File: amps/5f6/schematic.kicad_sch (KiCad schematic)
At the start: 69 parts, among them T3 2R sec

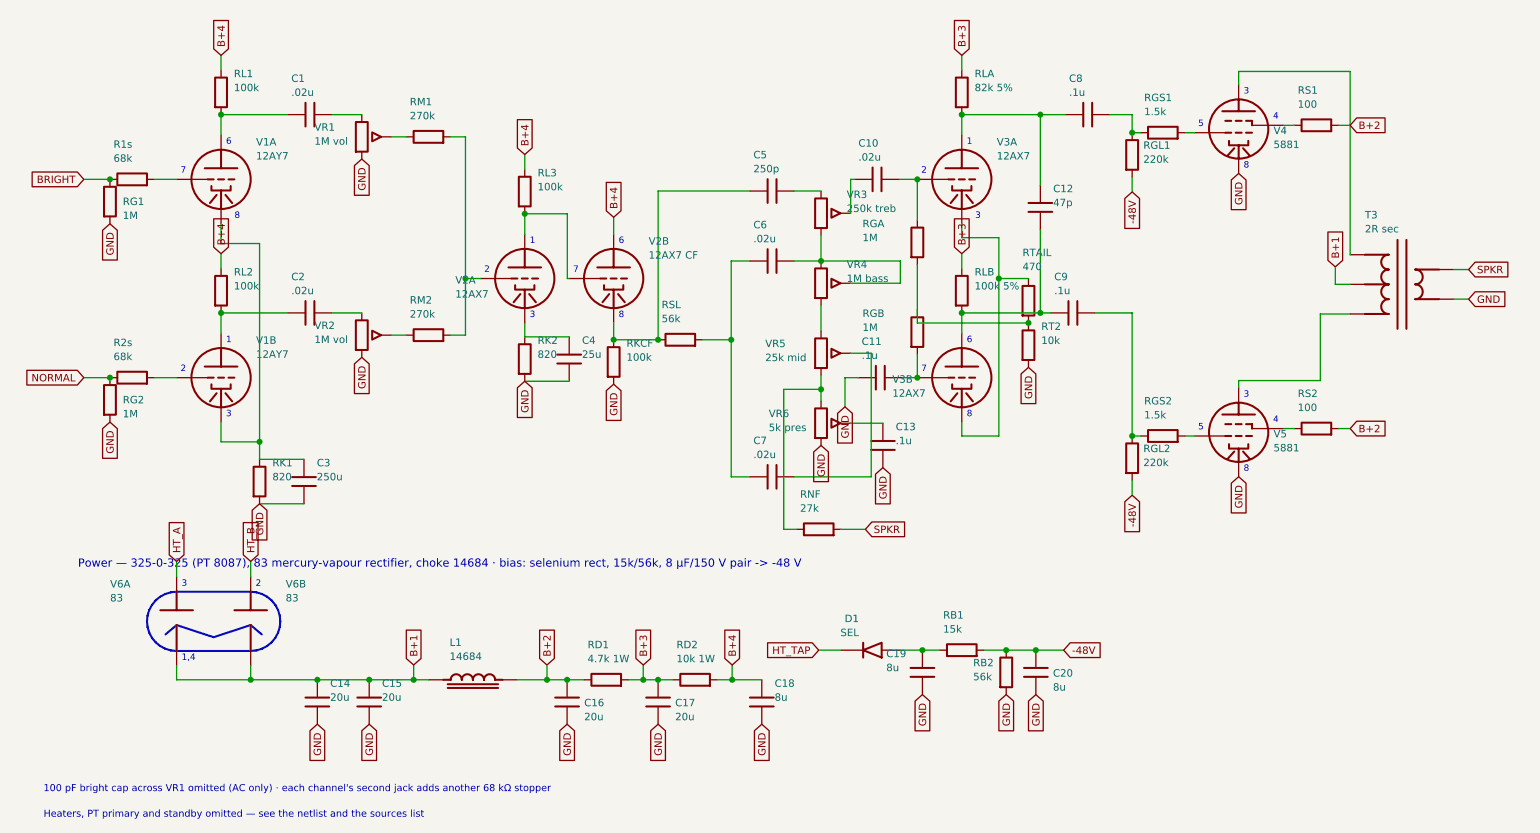
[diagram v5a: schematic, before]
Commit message: 5F6: each input jack has its own 68 kΩ stopper (V1 audit)
F-EG draws four input jacks and four 68 Ks, two per channel, on both pages
(schematic 6039x3508 crop 0,850,1300,2550; layout 6286x3564 crop
4950,450,6000,2250), with each channel's 1 MΩ leak at jack 1's tip. The
corpus carried one 68 K per channel, a simplification the BOM note and the
layout caption stated. R3s and R4s (68 k) are added to the BOM, the sheet
and the board (declared series_bridge); the board widens by two columns.
No DC node moves.

Co-Authored-By: Claude Opus 5.5 <noreply@anthropic.com>
Claude-Session: https://claude.ai/code/session_01KBMfdh37HmCL2iWcBiL5J1
Signed-off-by: AnalogMaker <theanalogmaker@gmail.com>
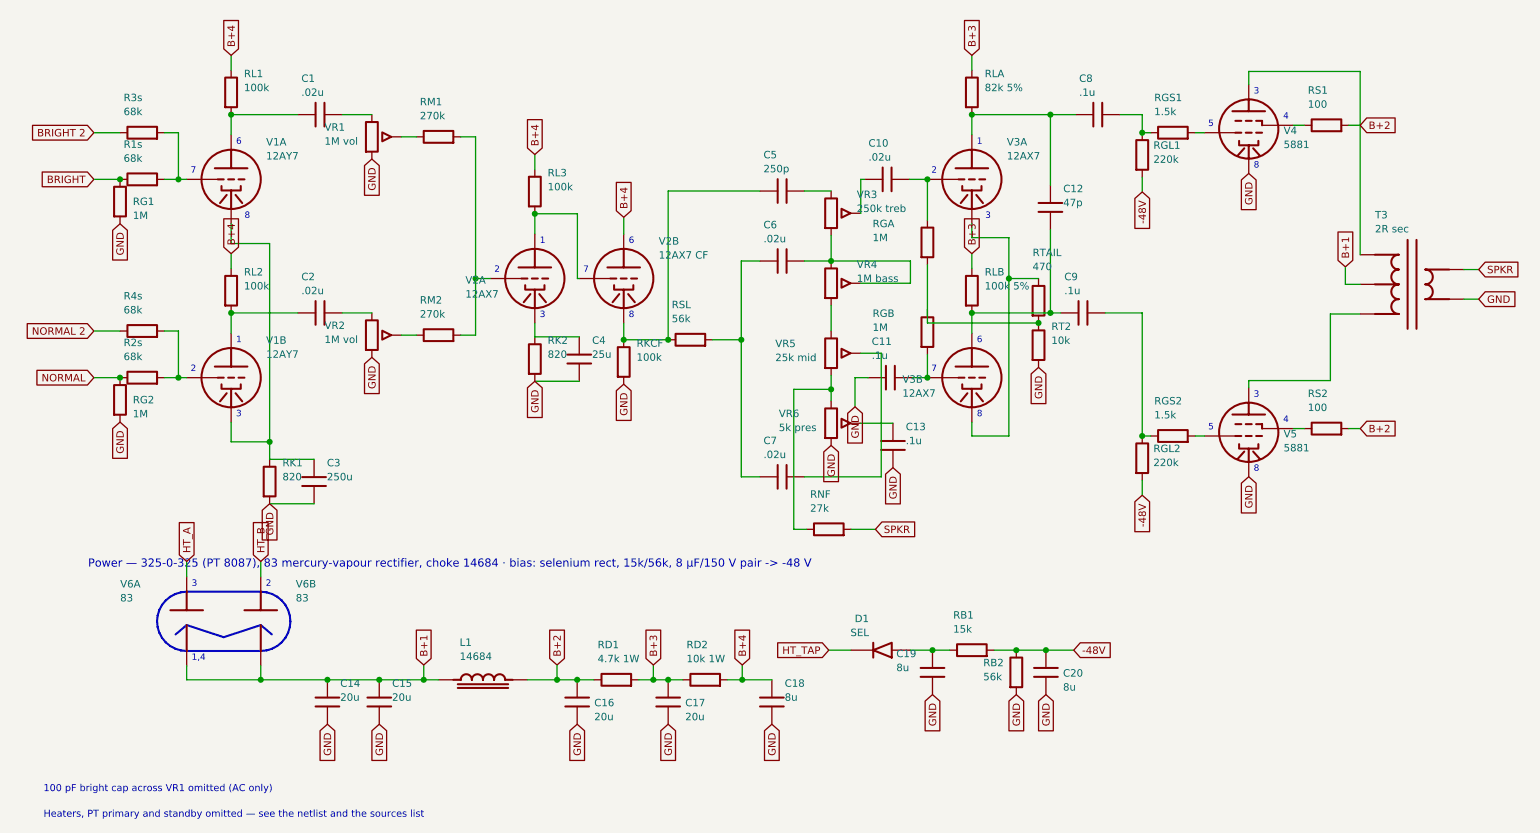
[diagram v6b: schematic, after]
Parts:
- removed C12: 47p, symbol cx:C
- removed C13: .1u, symbol cx:C
- removed D1: SEL, symbol cx:DIODE_SS
- removed RGS1: 1.5k, symbol cx:R
- removed RK1: 820, symbol cx:R
- removed RL1: 100k, symbol cx:R
- removed RLA: 82k 5%, symbol cx:R
- removed V2A: 12AX7, symbol cx:TRIODE
- added C20: 8u, symbol cx:C
- added C8, C9: .1u, symbol cx:C
- added R3s, R4s: 68k, symbol cx:R
- added RL3: 100k, symbol cx:R
- added V2B: 12AX7 CF, symbol cx:TRIODE
- added V3B: 12AX7, symbol cx:TRIODE
- added V5: 5881, symbol cx:PENTODE
- added VR1: 1M vol, symbol cx:POT
- C12: renamed from RGL1; value 220k -> 47p; symbol cx:R -> cx:C
- C13: renamed from V3B; value 12AX7 -> .1u; symbol cx:TRIODE -> cx:C; Basing_unit 1 -> (none)
- D1: renamed from C20; value 8u -> SEL; symbol cx:C -> cx:DIODE_SS
- RGB: renamed from C8; value .1u -> 1M; symbol cx:C -> cx:R
- RGL1: renamed from V5; value 5881 -> 220k; symbol cx:PENTODE -> cx:R
- RGS1: renamed from C9; value .1u -> 1.5k; symbol cx:C -> cx:R
- RK1: renamed from RL3; value 100k -> 820
- RL1: renamed from VR1; value 1M vol -> 100k; symbol cx:POT -> cx:R
- RLA: renamed from RTAIL; value 470 -> 82k 5%
- RTAIL: renamed from RGB; value 1M -> 470
- V2A: renamed from V2B; value 12AX7 CF -> 12AX7; Basing_unit 1 -> 2
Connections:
- net -48V: now also RGL1.2, C20.1; no longer C12.2, D1.1
- net B+3: now also RLA.1
- net B+4: now also RL1.1, RL3.1, V2B.1 (P); no longer RK1.1, V2A.1 (P)
- net GND: now also C13.2, RK1.2, C20.2, V5.4 (K), VR1.3; no longer D1.2, RGL1.4 (K), RL1.3
- net HT_TAP: now also D1.2 (K)
- net at RGB.2: now also C11.2, V3B.2 (G); no longer C12.1
- net at V4.2 (G1): now also RGS1.2
- net at R2s.2, V1B.2 (G): now also R4s.2
- net at C5.1, RKCF.1, RSL.1: now also V2B.3 (K); no longer V2A.3 (K)
- net at T3.3 (PRI_B): now also V5.1 (P); no longer RGL1.1 (P)
- net at RGS2.2: now also V5.2 (G1); no longer RGL1.2 (G1)
- net at RS2.1: now also V5.3 (G2); no longer RGL1.3 (G2)
- net at C1.1, V1A.1 (P): now also RL1.2
- net at V2A.2 (G): now also RM1.2, RM2.2; no longer RK1.2
- net at C4.1, RK2.1: now also V2A.3 (K)
- net at RGL2.1, RGS2.1: now also C9.2; no longer RGS1.2
- net at V3A.1 (P): now also C12.1, RLA.2, C8.1; no longer RGB.1
- net at R1s.2, V1A.2 (G): now also R3s.2
- net at C19.1, RB1.1: now also D1.1 (A)
- net at C1.2: now also VR1.1; no longer RL1.1
- net at RM1.1: now also VR1.2 (W); no longer RL1.2 (W)
- net at C3.1, V1A.3 (K), V1B.3 (K): now also RK1.1
- net at VR6.2 (W): now also C13.1
- net at RGA.2, RT2.1: now also RGB.1, RTAIL.2; no longer RLA.2, RTAIL.1
- new net: C8.2, RGL1.1, RGS1.1
- new net: C12.2, C9.1, RLB.2, V3B.1 (P)
- new net: RL3.2, V2A.1 (P), V2B.2 (G)
- new net: RTAIL.1, V3A.3 (K), V3B.3 (K)
- new net BRIGHT 2: R3s.1
- new net NORMAL 2: R4s.1
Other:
- note added: "100 pF bright cap across VR1 omitted (AC only)"
- note removed: "100 pF bright cap across VR1 omitted (AC only) · each channel's second jack adds another 68 kΩ stopper"
- moved on the sheet: D1, R1s, RK1, RLA, RTAIL, V1A, V2A
